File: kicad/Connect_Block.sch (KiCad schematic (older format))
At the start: 21 parts, among them CON601 AVR-ISP-6, IC601 ATTINY861A-S, P601 CONN_4X2, SW501 8Y1021, SW502 8Y1021, X601 20MHz

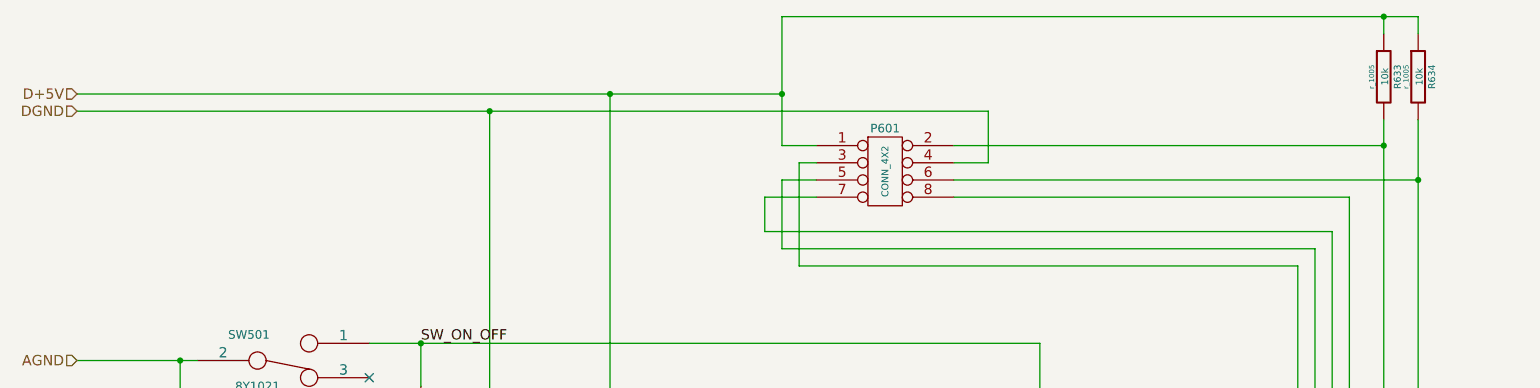
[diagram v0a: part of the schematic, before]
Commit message: Add: compander sch&pcb mod: constants
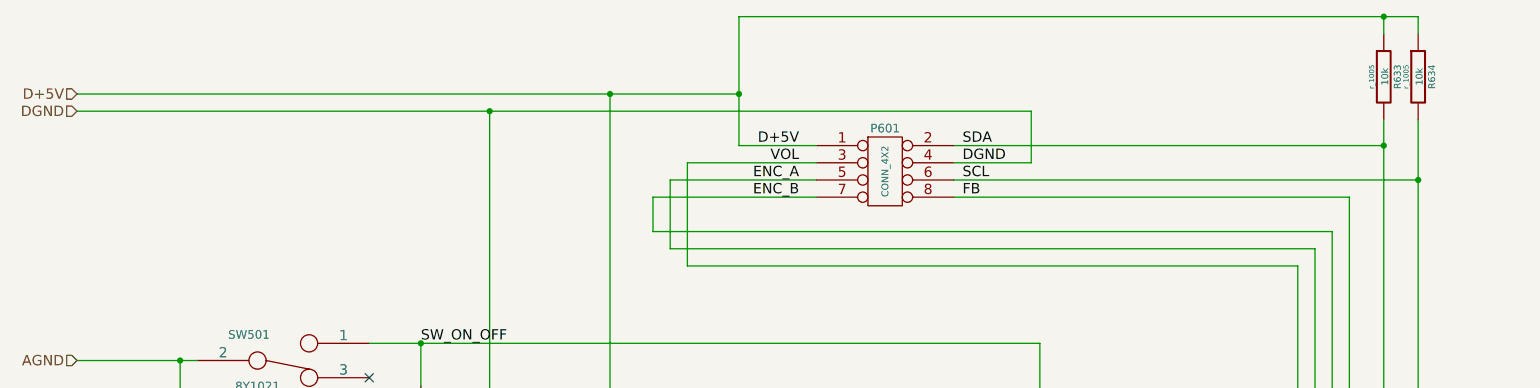
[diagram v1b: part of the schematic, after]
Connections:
- net VOL: now reaches C648.2, IC601.7 ((ADC7/~OC1D~/CLKI/XTAL1/PCINT12)PB4), P601.3, X601.1
- net FB: now reaches C649.2, IC601.8 ((ADC8/OC1D/CLKO/XTAL2/PCINT13)PB5), P601.8, X601.2
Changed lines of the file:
@@
 LIBS:jrc
 LIBS:rohm
+LIBS:temp
+LIBS:alps
+LIBS:on_semiconductor
 LIBS:AnalogDelay-cache
 EELAYER 27 0
@@
 Sheet 6 6
 Title ""
-Date "15 dec 2013"
+Date "30 apr 2014"
 Rev ""
 Comp ""
@@
 	8400 6450 10300 6450
 Wire Wire Line
-	7100 2700 7300 2700
-Wire Wire Line
-	7100 1950 7100 2700
-Wire Wire Line
-	8300 2500 8300 2800
-Wire Wire Line
-	3000 2500 8300 2500
-Wire Wire Line
-	3000 2400 7100 2400
+	6850 2700 7300 2700
+Wire Wire Line
+	6850 1950 6850 2700
+Wire Wire Line
+	8550 2500 8550 2800
+Wire Wire Line
+	3000 2500 8550 2500
+Wire Wire Line
+	3000 2400 6850 2400
 Wire Wire Line
 	10800 2550 10800 5450
@@
 	10800 2900 8100 2900
 Wire Wire Line
-	8300 2800 8100 2800
+	8550 2800 8100 2800
 Wire Wire Line
 	8100 2700 10600 2700
@@
 	10200 6350 10200 3300
 Wire Wire Line
-	10200 3300 7100 3300
-Wire Wire Line
-	7100 3300 7100 2900
-Wire Wire Line
-	7100 2900 7300 2900
+	10200 3300 6450 3300
+Wire Wire Line
+	6450 3300 6450 2900
+Wire Wire Line
+	6450 2900 7300 2900
 Wire Wire Line
 	10300 6450 10300 3200
 Wire Wire Line
-	10300 3200 7000 3200
-Wire Wire Line
-	7000 3200 7000 3000
-Wire Wire Line
-	7000 3000 7300 3000
+	10300 3200 6350 3200
+Wire Wire Line
+	6350 3200 6350 3000
+Wire Wire Line
+	6350 3000 7300 3000
 Connection ~ 6100 5650
 Wire Wire Line
@@
 	10600 2050 10600 1950
 Wire Wire Line
-	7100 1950 10800 1950
+	6850 1950 10800 1950
 Wire Wire Line
 	10800 1950 10800 2050
-Connection ~ 7100 2400
+Connection ~ 6850 2400
 Connection ~ 10600 1950
 Wire Wire Line
@@
 	10100 6550 10100 3400
 Wire Wire Line
-	10100 3400 7200 3400
-Wire Wire Line
-	7200 3400 7200 2800
-Wire Wire Line
-	7200 2800 7300 2800
+	10100 3400 6550 3400
+Wire Wire Line
+	6550 3400 6550 2800
+Wire Wire Line
+	6550 2800 7300 2800
 Connection ~ 10600 5250
 Connection ~ 10800 5450
@@
 	5000 4600 3600 4600
 Connection ~ 3600 4600
+Text Label 7200 2900 2    60   ~ 0
+ENC_A
+Text Label 7200 3000 2    60   ~ 0
+ENC_B
+Text Label 7200 2700 2    60   ~ 0
+D+5V
+Text Label 8150 2800 0    60   ~ 0
+DGND
+Text Label 8150 2700 0    60   ~ 0
+SDA
+Text Label 8150 2900 0    60   ~ 0
+SCL
+Text Label 8150 3000 0    60   ~ 0
+FB
+Text Label 7200 2800 2    60   ~ 0
+VOL
 $EndSCHEMATC

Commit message: mod: Schematics
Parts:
- removed C648, C649: 22p, c_1005, symbol C_1005
- removed X601: 20MHz, ~, symbol CRYSTAL
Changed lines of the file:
@@
 LIBS:jrc
 LIBS:rohm
-LIBS:temp
 LIBS:alps
 LIBS:on_semiconductor
@@
 $Descr A3 16535 11693
 encoding utf-8
-Sheet 6 6
+Sheet 8 8
 Title ""
-Date "30 apr 2014"
+Date "8 jun 2014"
 Rev ""
 Comp ""
@@
 	1    0    0    -1
 $EndComp
-$Comp
-L CRYSTAL X601
-U 1 1 52992B34
-P 9700 7100
-F 0 "X601" H 9700 7250 60  0000 C CNN
-F 1 "20MHz" H 9700 6950 60  0000 C CNN
-F 2 "~" H 9700 7100 60  0000 C CNN
-F 3 "~" H 9700 7100 60  0000 C CNN
-F 4 "DNP" H 9700 6850 60  0000 C CNN "Populate"
-	1    9700 7100
-	1    0    0    -1
-$EndComp
-Wire Wire Line
-	4700 3850 8600 3850
-Wire Wire Line
-	4700 4950 8700 4950
-Wire Wire Line
-	3000 3950 3700 3950
+Wire Wire Line
+	4700 3850 5000 3850
+Wire Wire Line
+	5000 3850 8600 3850
+Wire Wire Line
+	4700 4950 5000 4950
+Wire Wire Line
+	5000 4950 8700 4950
+Wire Wire Line
+	3000 3950 3600 3950
+Wire Wire Line
+	3600 3950 3700 3950
 Wire Wire Line
 	3600 5050 3700 5050
 Connection ~ 3600 3950
 Wire Wire Line
-	8400 6350 10200 6350
-Wire Wire Line
-	9300 5450 11300 5450
-Wire Wire Line
-	9300 5250 11300 5250
+	8400 6350 8900 6350
+Wire Wire Line
+	8900 6350 10200 6350
+Wire Wire Line
+	9300 5450 10800 5450
+Wire Wire Line
+	10800 5450 11300 5450
+Wire Wire Line
+	9300 5250 10600 5250
+Wire Wire Line
+	10600 5250 11300 5250
 Wire Wire Line
 	5400 6850 6200 6850
 Wire Wire Line
-	5400 2500 5400 7850
+	5400 2500 5400 5250
+Wire Wire Line
+	5400 5250 5400 5650
+Wire Wire Line
+	5400 5650 5400 6450
+Wire Wire Line
+	5400 6450 5400 6850
+Wire Wire Line
+	5400 6850 5400 7850
 Wire Wire Line
 	5400 6450 6200 6450
 Wire Wire Line
-	5950 5650 6200 5650
-Wire Wire Line
-	6100 2400 6100 8800
-Wire Wire Line
-	5950 5250 6200 5250
+	5950 5650 6100 5650
+Wire Wire Line
+	6100 5650 6200 5650
+Wire Wire Line
+	6100 2400 6100 5250
+Wire Wire Line
+	6100 5250 6100 5650
+Wire Wire Line
+	6100 5650 6100 7250
+Wire Wire Line
+	6100 7250 6100 8800
+Wire Wire Line
+	5950 5250 6100 5250
+Wire Wire Line
+	6100 5250 6200 5250
 Wire Wire Line
 	8700 4950 8700 5950
@@
 	6850 2700 7300 2700
 Wire Wire Line
-	6850 1950 6850 2700
+	6850 1950 6850 2400
+Wire Wire Line
+	6850 2400 6850 2700
 Wire Wire Line
 	8550 2500 8550 2800
 Wire Wire Line
-	3000 2500 8550 2500
-Wire Wire Line
-	3000 2400 6850 2400
-Wire Wire Line
-	10800 2550 10800 5450
+	3000 2500 5400 2500
+Wire Wire Line
+	5400 2500 8550 2500
+Wire Wire Line
+	3000 2400 6100 2400
+Wire Wire Line
+	6100 2400 6850 2400
+Wire Wire Line
+	10800 2550 10800 2900
+Wire Wire Line
+	10800 2900 10800 5450
 Wire Wire Line
 	10800 2900 8100 2900
@@
 	8100 2700 10600 2700
 Wire Wire Line
-	10600 2550 10600 5250
+	10600 2550 10600 2700
+Wire Wire Line
+	10600 2700 10600 5250
 Wire Wire Line
 	10400 3000 8100 3000
@@
 	10600 2050 10600 1950
 Wire Wire Line
-	6850 1950 10800 1950
+	6850 1950 10600 1950
+Wire Wire Line
+	10600 1950 10800 1950
 Wire Wire Line
 	10800 1950 10800 2050
@@
 Connection ~ 10600 1950
 Wire Wire Line
-	8400 6150 9125 6150
-Wire Wire Line
-	8400 6250 9125 6250
+	8400 6150 9050 6150
+Wire Wire Line
+	9050 6150 9125 6150
+Wire Wire Line
+	8400 6250 8975 6250
+Wire Wire Line
+	8975 6250 9125 6250
 Wire Wire Line
 	8400 5250 8800 5250
@@
 	8400 6850 8600 6850
 Wire Wire Line
-	8600 6850 8600 8350
-Wire Wire Line
-	7450 7250 8600 7250
+	8600 6850 8600 7250
+Wire Wire Line
+	8600 7250 8600 8350
+Wire Wire Line
+	7450 7250 7700 7250
+Wire Wire Line
+	7700 7250 8600 7250
 Wire Wire Line
 	6100 7250 6950 7250
@@
 Connection ~ 7700 7250
 Wire Wire Line
-	7700 7750 7700 8875
-Wire Wire Line
-	5400 7850 8000 7850
+	7700 7750 7700 7850
+Wire Wire Line
+	7700 7850 7700 8875
+Wire Wire Line
+	5400 7850 7700 7850
 Connection ~ 5400 6850
 Wire Wire Line
@@
 Connection ~ 10800 5450
 Wire Wire Line
-	8400 6550 10100 6550
-Wire Wire Line
-	8400 6650 10400 6650
+	8400 6550 9300 6550
+Wire Wire Line
+	9300 6550 10100 6550
+Wire Wire Line
+	8400 6650 10100 6650
+Wire Wire Line
+	10100 6650 10400 6650
 Wire Wire Line
 	8975 8150 10425 8150
@@
 	8900 8250 8900 6350
 Connection ~ 8900 6350
-Wire Wire Line
-	9400 7100 9300 7100
-Wire Wire Line
-	9300 6550 9300 7200
-Connection ~ 9300 6550
-Wire Wire Line
-	10000 7100 10100 7100
-Wire Wire Line
-	10100 6650 10100 7200
-Connection ~ 10100 6650
-$Comp
-L C_1005 C649
-U 1 1 52992D4E
-P 10100 7400
-F 0 "C649" H 10100 7575 40  0000 C CNN
-F 1 "22p" H 10100 7525 40  0000 C CNN
-F 2 "c_1005" H 10100 7275 30  0000 C CNN
-F 3 "~" V 10100 7400 60  0000 C CNN
-F 4 "DNP" H 10100 7200 60  0000 C CNN "Populate"
-	1    10100 7400
-	0    -1   -1   0
-$EndComp
-Connection ~ 10100 7100
-Connection ~ 9300 7100
-Wire Wire Line
-	9300 7600 9300 7700
-Wire Wire Line
-	8000 7700 10100 7700
-Wire Wire Line
-	10100 7700 10100 7600
-Wire Wire Line
-	8000 7850 8000 7700
-Connection ~ 9300 7700
-$Comp
-L C_1005 C648
-U 1 1 52992FD9
-P 9300 7400
-F 0 "C648" H 9300 7575 40  0000 C CNN
-F 1 "22p" H 9300 7525 40  0000 C CNN
-F 2 "c_1005" H 9300 7275 30  0000 C CNN
-F 3 "~" V 9300 7400 60  0000 C CNN
-F 4 "DNP" H 9300 7200 60  0000 C CNN "Populate"
-	1    9300 7400
-	0    -1   -1   0
-$EndComp
 Wire Wire Line
 	8400 6750 10550 6750
@@
 ON_OFF
 Wire Wire Line
-	3600 3950 3600 5650
+	3600 3950 3600 4600
+Wire Wire Line
+	3600 4600 3600 5050
+Wire Wire Line
+	3600 5050 3600 5650
 Text HLabel 3000 3950 0    60   Input ~ 0
 AGND
